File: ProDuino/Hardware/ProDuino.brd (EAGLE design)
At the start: 57.7 x 53.3 mm, 36 parts, among them J1 Digital, J2 Analog, J4 POWER, J5 Digital, Q1 RESONATORSMD, SW1 SPST_TACT-EVQQ2, U1 ATMEGA328, U2 3.3V

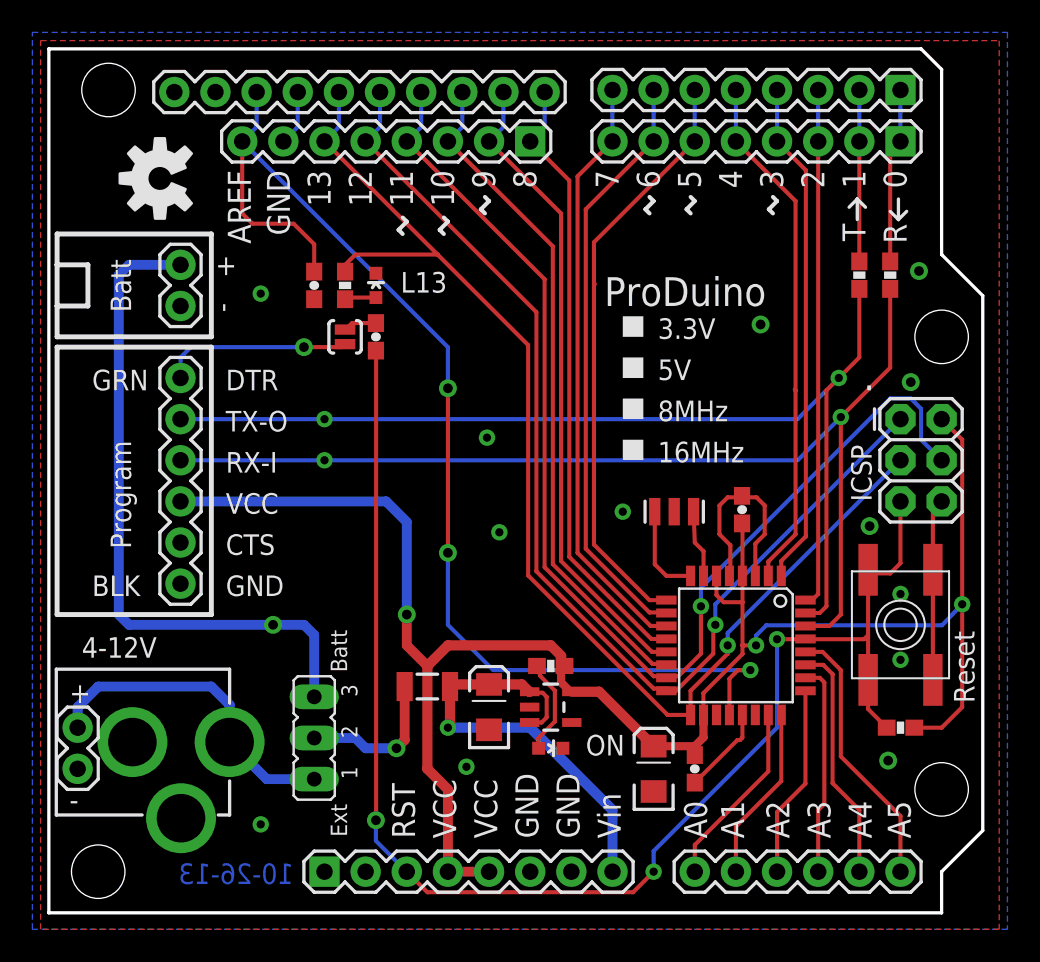
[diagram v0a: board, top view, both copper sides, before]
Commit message: Fix ProDuino v1 non-consistent
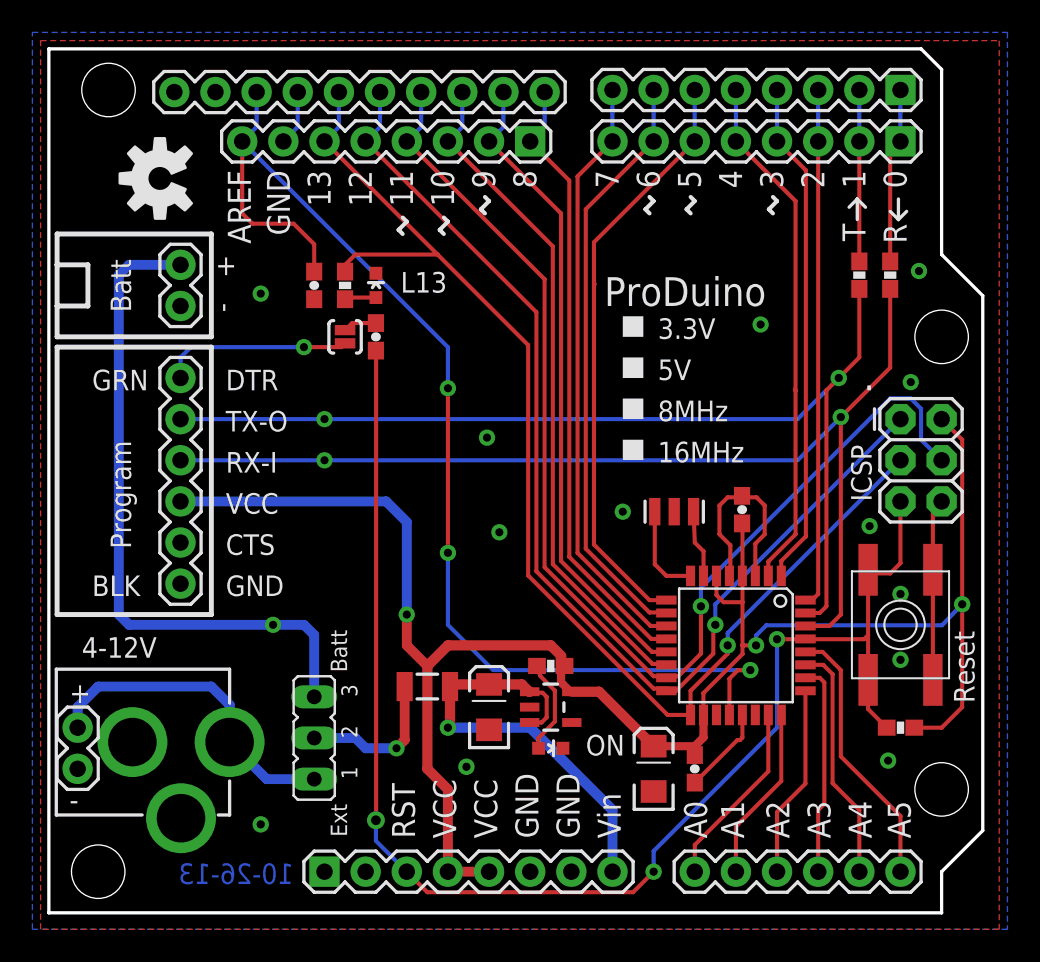
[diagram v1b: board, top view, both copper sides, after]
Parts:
- SJ1: device SparkFun-Capacitors:SJ_2S-NO -> SparkFun-Capacitors:SJ_2S-NOTRACE
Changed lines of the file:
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@@
 <?xml version="1.0" encoding="utf-8"?>
 <!DOCTYPE eagle SYSTEM "eagle.dtd">
-<eagle version="6.4">
+<eagle version="6.5.0">
 <drawing>
 <settings>
@@
 <setting verticaltext="up"/>
 </settings>
-<grid distance="20" unitdist="mil" unit="mil" style="lines" multiple="1" display="yes" altdistance="0.025" altunitdist="inch" altunit="inch"/>
+<grid distance="20" unitdist="mil" unit="mm" style="lines" multiple="1" display="yes" altdistance="0.025" altunitdist="inch" altunit="inch"/>
 <layers>
 <layer number="1" name="Top" color="4" fill="1" visible="yes" active="yes"/>
@@
 <param name="rvMicroViaOuter" value="0.25"/>
 <param name="rvMicroViaInner" value="0.25"/>
-<param name="rlMinPadTop" value="12mil"/>
+<param name="rlMinPadTop" value="10mil"/>
 <param name="rlMaxPadTop" value="20mil"/>
 <param name="rlMinPadInner" value="10mil"/>
 <param name="rlMaxPadInner" value="20mil"/>
-<param name="rlMinPadBottom" value="12mil"/>
+<param name="rlMinPadBottom" value="10mil"/>
 <param name="rlMaxPadBottom" value="20mil"/>
 <param name="rlMinViaOuter" value="10mil"/>
@@
 <element name="Q1" library="SparkFun" package="RESONATOR-SMD" value="RESONATORSMD" x="38.1" y="24.765" smashed="yes"/>
 <element name="C2" library="SparkFun-Capacitors" package="0603-CAP" value="0.1uF" x="19.685" y="35.56" smashed="yes" rot="R270"/>
-<element name="SJ1" library="SparkFun-Capacitors" package="SJ_2S-NO" value="SOLDERJUMPERNC3" x="17.78" y="35.56" smashed="yes" rot="R90"/>
+<element name="SJ1" library="SparkFun-Capacitors" package="SJ_2S-NOTRACE" value="SOLDERJUMPERNC3" x="17.78" y="35.56" smashed="yes" rot="R90"/>
 <element name="JP9" library="SparkFun" package="1X06" value="Program" x="7.62" y="33.02" smashed="yes" rot="R270"/>
 <element name="U1" library="SparkFun" package="TQFP32-08" value="ATMEGA328" x="41.91" y="16.51" smashed="yes" rot="R270"/>
@@
 <contactref element="U1" pad="21"/>
 <contactref element="U1" pad="3"/>
-<via x="34.925" y="24.765" extent="1-16" drill="0.508"/>
-<via x="27.305" y="23.495" extent="1-16" drill="0.508"/>
+<via x="34.925" y="24.765" extent="1-16" drill="0.5"/>
+<via x="27.305" y="23.495" extent="1-16" drill="0.5"/>
 <via x="52.07" y="15.621" extent="1-16" drill="0.508"/>
 <polygon width="0.254" layer="1" isolate="0.508">
@@
 <wire x1="54.07" y1="21.18" x2="54.07" y2="24.86" width="0.254" layer="1"/>
 <wire x1="54.07" y1="24.86" x2="54.61" y2="25.4" width="0.254" layer="1"/>
-<via x="50.165" y="23.876" extent="1-16" drill="0.6"/>
+<via x="50.165" y="23.876" extent="1-16" drill="0.5"/>
 <contactref element="J4" pad="7"/>
 <contactref element="J4" pad="6"/>
@@
 <wire x1="42.164" y1="10.668" x2="41.998" y2="10.668" width="0.254" layer="1"/>
 <wire x1="41.998" y1="10.668" x2="39.37" y2="8.04" width="0.254" layer="1"/>
-<via x="43.434" y="36.322" extent="1-16" drill="0.6"/>
-<via x="51.308" y="9.398" extent="1-16" drill="0.6"/>
+<via x="43.434" y="36.322" extent="1-16" drill="0.5"/>
+<via x="51.308" y="9.398" extent="1-16" drill="0.5"/>
 <via x="52.07" y="19.685" extent="1-16" drill="0.508"/>
 <wire x1="43.11" y1="20.8026" x2="43.11" y2="22.79" width="0.254" layer="1"/>
@@
 <wire x1="41.402" y1="25.654" x2="42.203" y2="25.654" width="0.254" layer="1"/>
 <wire x1="42.203" y1="25.654" x2="42.291" y2="25.742" width="0.254" layer="1"/>
-<via x="26.543" y="29.337" extent="1-16" drill="0.508"/>
+<via x="26.543" y="29.337" extent="1-16" drill="0.5"/>
 <via x="12.573" y="5.461" extent="1-16" drill="0.508"/>
 <via x="25.273" y="9.017" extent="1-16" drill="0.508"/>
-<via x="12.573" y="38.227" extent="1-16" drill="0.508"/>
-<via x="53.213" y="39.624" extent="1-16" drill="0.6"/>
-<via x="52.705" y="32.766" extent="1-16" drill="0.6"/>
+<via x="12.573" y="38.227" extent="1-16" drill="0.5"/>
+<via x="53.213" y="39.624" extent="1-16" drill="0.5"/>
+<via x="52.705" y="32.766" extent="1-16" drill="0.5"/>
 </signal>
 <signal name="AREF">
@@
 <via x="42.799" y="14.986" extent="1-16" drill="0.508"/>
 <wire x1="24.13" y1="17.78" x2="24.13" y2="22.225" width="0.254" layer="16"/>
-<via x="24.13" y="22.225" extent="1-16" drill="0.6"/>
+<via x="24.13" y="22.225" extent="1-16" drill="0.5"/>
 <wire x1="24.13" y1="22.225" x2="24.13" y2="32.385" width="0.254" layer="1"/>
-<via x="24.13" y="32.385" extent="1-16" drill="0.6"/>
+<via x="24.13" y="32.385" extent="1-16" drill="0.5"/>
 <wire x1="24.13" y1="32.385" x2="24.13" y2="34.925" width="0.254" layer="16"/>
 <contactref element="J5" pad="8"/>
@@
 <wire x1="21.46" y1="13.97" x2="21.46" y2="10.665" width="0.6096" layer="1"/>
 <wire x1="21.46" y1="10.665" x2="20.955" y2="10.16" width="0.6096" layer="1"/>
-<via x="20.955" y="10.16" extent="1-16" drill="0.6"/>
+<via x="20.955" y="10.16" extent="1-16" drill="0.5"/>
 <wire x1="15.875" y1="10.795" x2="18.415" y2="10.795" width="0.6096" layer="16"/>
 <wire x1="18.415" y1="10.795" x2="19.05" y2="10.16" width="0.6096" layer="16"/>
@@
 <wire x1="22.86" y1="15.24" x2="21.59" y2="16.51" width="0.6096" layer="1"/>
 <wire x1="21.59" y1="16.51" x2="21.59" y2="18.415" width="0.6096" layer="1"/>
-<via x="21.59" y="18.415" extent="1-16" drill="0.6"/>
+<via x="21.59" y="18.415" extent="1-16" drill="0.5"/>
 <wire x1="21.59" y1="18.415" x2="21.59" y2="24.13" width="0.6096" layer="16"/>
 <wire x1="21.59" y1="24.13" x2="20.32" y2="25.4" width="0.6096" layer="16"/>
@@
 <wire x1="3.81" y1="18.415" x2="4.445" y2="17.78" width="0.6096" layer="16"/>
 <wire x1="4.445" y1="17.78" x2="13.335" y2="17.78" width="0.6096" layer="16"/>
-<via x="13.335" y="17.78" extent="1-16" drill="0.6"/>
+<via x="13.335" y="17.78" extent="1-16" drill="0.5"/>
 <wire x1="13.335" y1="17.78" x2="15.24" y2="17.78" width="0.6096" layer="16"/>
 <wire x1="15.24" y1="17.78" x2="15.875" y2="17.145" width="0.6096" layer="16"/>
@@
 <wire x1="16.51" y1="27.94" x2="45.72" y2="27.94" width="0.254" layer="16"/>
 <wire x1="45.72" y1="27.94" x2="48.387" y2="30.607" width="0.254" layer="16"/>
-<via x="16.51" y="27.94" extent="1-16" drill="0.508"/>
+<via x="16.51" y="27.94" extent="1-16" drill="0.5"/>
 <via x="48.387" y="30.607" extent="1-16" drill="0.508"/>
 <wire x1="7.62" y1="27.94" x2="16.51" y2="27.94" width="0.254" layer="16"/>
@@
 <wire x1="48.26" y1="33.02" x2="47.498" y2="32.258" width="0.254" layer="1"/>
 <wire x1="47.498" y1="32.258" x2="47.498" y2="18.923" width="0.254" layer="1"/>
-<via x="16.51" y="30.48" extent="1-16" drill="0.508"/>
+<via x="16.51" y="30.48" extent="1-16" drill="0.5"/>
 <via x="48.26" y="33.02" extent="1-16" drill="0.508"/>
 <wire x1="7.62" y1="30.48" x2="16.51" y2="30.48" width="0.254" layer="16"/>
@@
 <contactref element="SJ1" pad="2"/>
 <wire x1="19.685" y1="36.41" x2="18.2173" y2="36.41" width="0.254" layer="1"/>
-<wire x1="18.2173" y1="36.41" x2="17.78" y2="36.01" width="0.254" layer="1"/>
+<wire x1="18.2173" y1="36.41" x2="17.78" y2="35.9727" width="0.254" layer="1"/>
 </signal>
 <signal name="DTR">
@@
 <wire x1="7.62" y1="34.29" x2="8.255" y2="34.925" width="0.254" layer="16"/>
 <wire x1="8.255" y1="34.925" x2="15.24" y2="34.925" width="0.254" layer="16"/>
-<via x="15.24" y="34.925" extent="1-16" drill="0.6"/>
+<via x="15.24" y="34.925" extent="1-16" drill="0.5"/>
 <wire x1="15.24" y1="34.925" x2="17.5459" y2="34.925" width="0.254" layer="1"/>
-<wire x1="17.5459" y1="34.925" x2="17.78" y2="35.11" width="0.254" layer="1"/>
+<wire x1="17.5459" y1="34.925" x2="17.78" y2="35.1591" width="0.254" layer="1"/>
 </signal>
 </signals>
